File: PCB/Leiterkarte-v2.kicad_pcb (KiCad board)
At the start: 4 copper layers, 69.2 x 70 mm, 56 parts

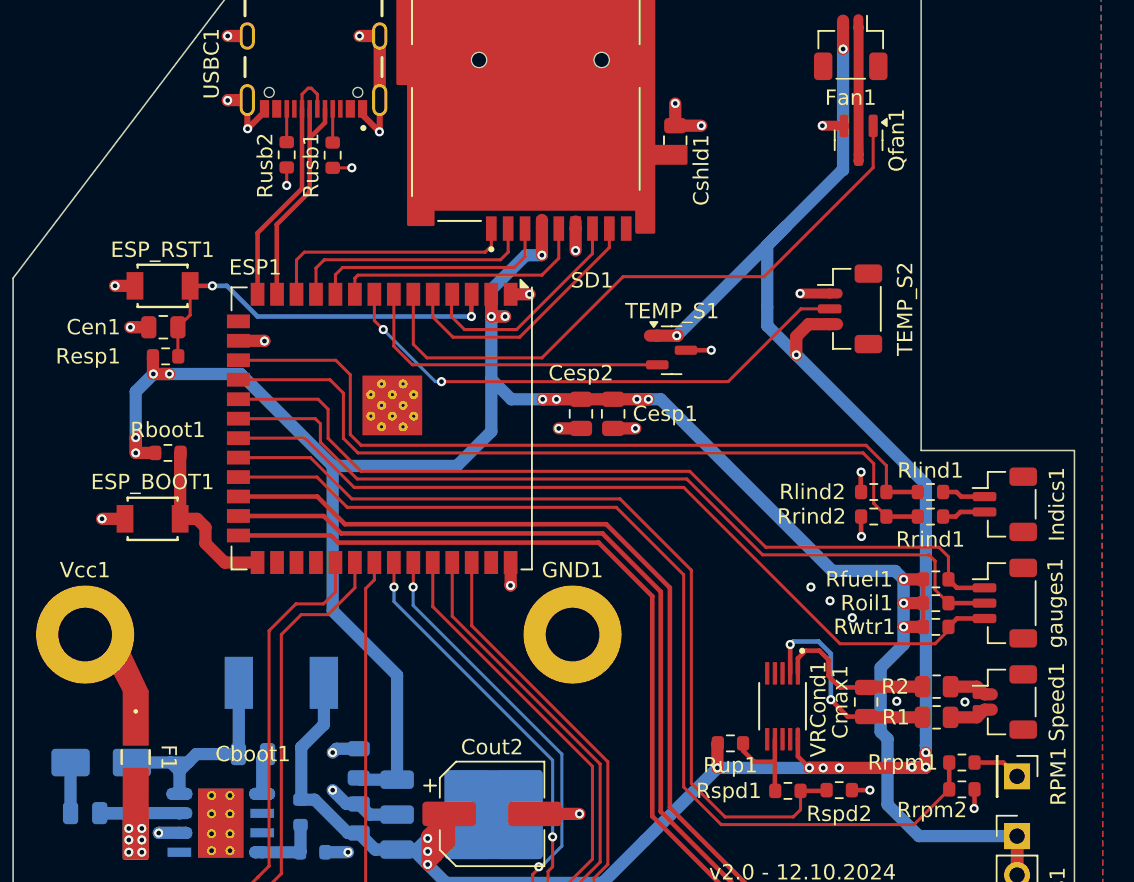
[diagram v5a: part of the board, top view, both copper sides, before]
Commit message: Replaced Fuse;Updated BOM file
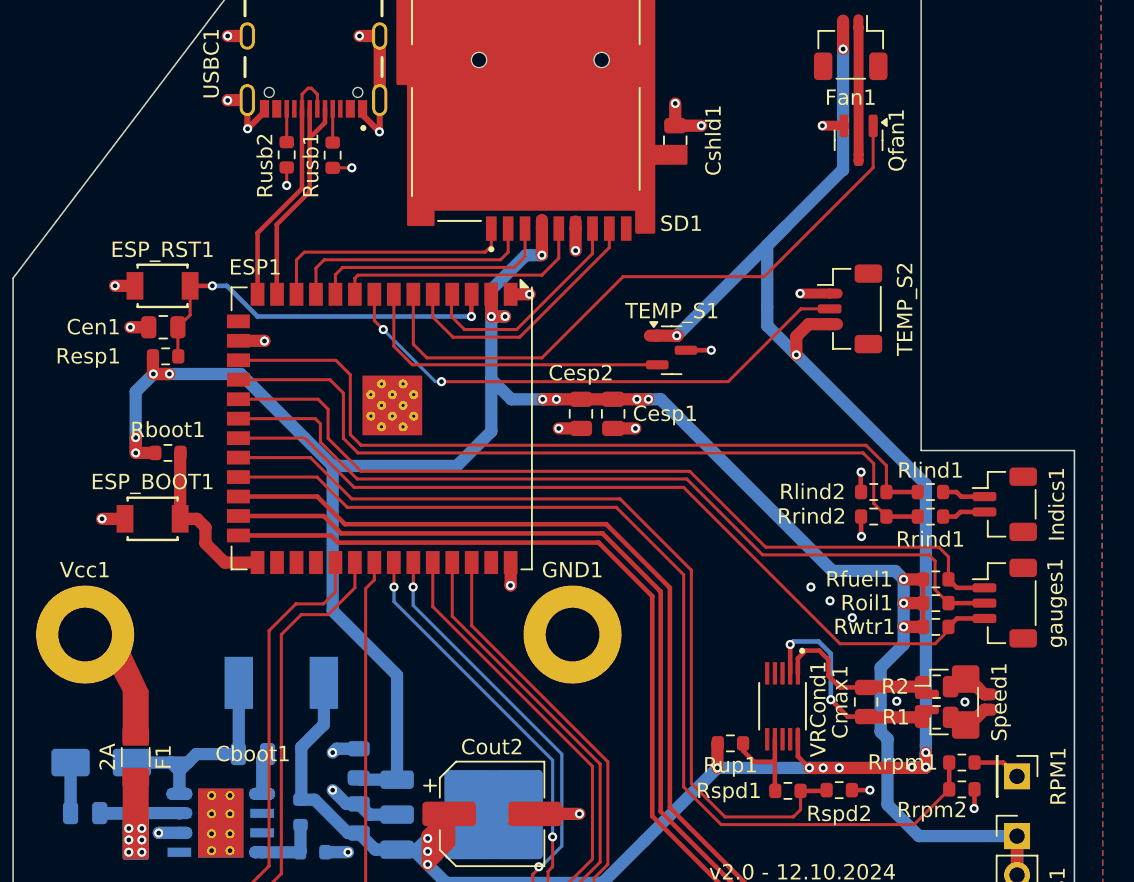
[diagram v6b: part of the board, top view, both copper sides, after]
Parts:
- F1: value 1.5A -> 2A; footprint Fuse:0458Series_LTF-M -> Fuse:Fuse_1206_3216Metric
- moved Speed1 3.75 mm to (146.5, 94.7)
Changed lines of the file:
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@@
 		)
 	)
-	(footprint "Fuse:0458Series_LTF-M"
+	(footprint "Fuse:Fuse_1206_3216Metric"
 		(layer "F.Cu")
 		(at 93.6 98.2468 -90)
-		(tags "0458002.DR ")
+		(descr "Fuse SMD 1206 (3216 Metric), square (rectangular) end terminal, IPC_7351 nominal, (Body size source: http://www.tortai-tech.com/upload/download/2011102023233369053.pdf), generated with kicad-footprint-generator")
+		(tags "fuse")
 		(property "Reference" "F1"
-			(at -0.0032 -2.15 -90)
-			(unlocked yes)
+			(at 0 -1.82 90)
 			(layer "F.SilkS")
 			(effects
@@
 			)
 		)
-		(property "Value" "1.5A"
-			(at 0 0 -90)
-			(unlocked yes)
-			(layer "F.Fab")
+		(property "Value" "2A"
+			(at 0 1.82 90)
+			(layer "F.SilkS")
 			(effects
 				(font
@@
 			)
 		)
-		(property "Footprint" "Fuse:0458Series_LTF-M"
-			(at 0 0 90)
+		(property "Footprint" "Fuse:Fuse_1206_3216Metric"
+			(at 0 0 -90)
+			(unlocked yes)
 			(layer "F.Fab")
 			(hide yes)
@@
 		)
 		(property "Datasheet" ""
-			(at 0 0 90)
+			(at 0 0 -90)
+			(unlocked yes)
 			(layer "F.Fab")
 			(hide yes)
@@
 		)
 		(property "Description" "Fuse"
-			(at 0 0 90)
+			(at 0 0 -90)
+			(unlocked yes)
 			(layer "F.Fab")
 			(hide yes)
@@
 		(attr smd)
 		(fp_line
-			(start -0.457851 0.9144)
-			(end 0.457851 0.9144)
+			(start -0.602064 0.91)
+			(end 0.602064 0.91)
 			(stroke
-				(width 0.1524)
+				(width 0.12)
 				(type solid)
 			)
@@
 		)
 		(fp_line
-			(start 0.457851 -0.9144)
-			(end -0.457851 -0.9144)
-			(stroke
-				(width 0.1524)
-				(type solid)
-			)
-			(layer "F.SilkS")
-		)
-		(fp_circle
-			(center -2.9845 0)
-			(end -2.9083 0)
+			(start -0.602064 -0.91)
+			(end 0.602064 -0.91)
 			(stroke
-				(width 0.1524)
+				(width 0.12)
 				(type solid)
 			)
-			(fill none)
 			(layer "F.SilkS")
 		)
 		(fp_line
-			(start -2.6543 1.3208)
-			(end -2.6543 -1.3208)
+			(start -2.28 1.12)
+			(end -2.28 -1.12)
 			(stroke
-				(width 0.1524)
+				(width 0.05)
 				(type solid)
 			)
@@
 		)
 		(fp_line
-			(start 2.6543 1.3208)
-			(end -2.6543 1.3208)
+			(start 2.28 1.12)
+			(end -2.28 1.12)
 			(stroke
-				(width 0.1524)
+				(width 0.05)
 				(type solid)
 			)
@@
 		)
 		(fp_line
-			(start -2.6543 -1.3208)
-			(end 2.6543 -1.3208)
+			(start -2.28 -1.12)
+			(end 2.28 -1.12)
 			(stroke
-				(width 0.1524)
+				(width 0.05)
 				(type solid)
 			)
@@
 		)
 		(fp_line
-			(start 2.6543 -1.3208)
-			(end 2.6543 1.3208)
+			(start 2.28 -1.12)
+			(end 2.28 1.12)
 			(stroke
-				(width 0.1524)
+				(width 0.05)
 				(type solid)
 			)
@@
 		)
 		(fp_line
-			(start -1.5875 0.7874)
-			(end -0.7747 0.7874)
-			(stroke
-				(width 0.0254)
-				(type solid)
-			)
-			(layer "F.Fab")
-		)
-		(fp_line
-			(start -1.5875 0.7874)
-			(end 1.5875 0.7874)
-			(stroke
-				(width 0.0254)
-				(type solid)
-			)
-			(layer "F.Fab")
-		)
-		(fp_line
-			(start -0.7747 0.7874)
-			(end -0.7747 -0.7874)
-			(stroke
-				(width 0.0254)
-				(type solid)
-			)
-			(layer "F.Fab")
-		)
-		(fp_line
-			(start 0.7747 0.7874)
-			(end 1.5875 0.7874)
-			(stroke
-				(width 0.0254)
-				(type solid)
-			)
-			(layer "F.Fab")
-		)
-		(fp_line
-			(start 1.5875 0.7874)
-			(end 1.5875 -0.7874)
-			(stroke
-				(width 0.0254)
-				(type solid)
-			)
-			(layer "F.Fab")
-		)
-		(fp_line
-			(start 1.5875 0.7874)
-			(end 1.5875 -0.7874)
-			(stroke
-				(width 0.0254)
-				(type solid)
-			)
-			(layer "F.Fab")
-		)
-		(fp_line
-			(start -1.5875 -0.7874)
-			(end -1.5875 0.7874)
+			(start -1.6 0.8)
+			(end -1.6 -0.8)
 			(stroke
-				(width 0.0254)
-				(type solid)
-			)
-			(layer "F.Fab")
-		)
-		(fp_line
-			(start -1.5875 -0.7874)
-			(end -1.5875 0.7874)
-			(stroke
-				(width 0.0254)
-				(type solid)
-			)
-			(layer "F.Fab")
-		)
-		(fp_line
-			(start -0.7747 -0.7874)
-			(end -1.5875 -0.7874)
-			(stroke
-				(width 0.0254)
+				(width 0.1)
 				(type solid)
 			)
@@
 		)
 		(fp_line
-			(start 0.7747 -0.7874)
-			(end 0.7747 0.7874)
+			(start 1.6 0.8)
+			(end -1.6 0.8)
 			(stroke
-				(width 0.0254)
+				(width 0.1)
 				(type solid)
 			)
@@
 		)
 		(fp_line
-			(start 1.5875 -0.7874)
-			(end -1.5875 -0.7874)
+			(start -1.6 -0.8)
+			(end 1.6 -0.8)
 			(stroke
-				(width 0.0254)
+				(width 0.1)
 				(type solid)
 			)
@@
 		)
 		(fp_line
-			(start 1.5875 -0.7874)
-			(end 0.7747 -0.7874)
+			(start 1.6 -0.8)
+			(end 1.6 0.8)
 			(stroke
-				(width 0.0254)
-				(type solid)
-			)
-			(layer "F.Fab")
-		)
-		(fp_circle
-			(center -1.3335 0)
-			(end -1.2573 0)
-			(stroke
-				(width 0.0254)
+				(width 0.1)
 				(type solid)
 			)
-			(fill none)
 			(layer "F.Fab")
 		)
 		(fp_text user "${REFERENCE}"
-			(at 0 0 -90)
-			(unlocked yes)
+			(at 0 0 90)
 			(layer "F.Fab")
 			(effects
 				(font
-					(size 1 1)
-					(thickness 0.15)
+					(size 0.8 0.8)
+					(thickness 0.12)
 				)
 			)
 		)
-		(pad "1" smd rect
-			(at -1.4605 0 270)
-			(size 1.3716 1.6256)
+		(pad "1" smd roundrect
+			(at -1.4 0 270)
+			(size 1.25 1.75)
 			(layers "F.Cu" "F.Paste" "F.Mask")
+			(roundrect_rratio 0.2)
 			(net 42 "Net-(Vcc1-Pin_1)")
 			(pintype "passive")
 		)
-		(pad "2" smd rect
-			(at 1.4605 0 270)
-			(size 1.3716 1.6256)
+		(pad "2" smd roundrect
+			(at 1.4 0 270)
+			(size 1.25 1.75)
 			(layers "F.Cu" "F.Paste" "F.Mask")
+			(roundrect_rratio 0.2)
 			(net 21 "VCC")
 			(pintype "passive")
 		)
-		(zone
-			(net 0)
-			(net_name "")
-			(layer "F.Cu")
-			(hatch full 0.508)
-			(connect_pads
-				(clearance 0)
-			)
-			(min_thickness 0.254)
-			(filled_areas_thickness no)
-			(keepout
-				(tracks not_allowed)
-				(vias not_allowed)
-				(pads allowed)
-				(copperpour not_allowed)
-				(footprints allowed)
-			)
-			(fill
-				(thermal_gap 0.508)
-				(thermal_bridge_width 0.508)
-			)
-			(polygon
-				(pts
-					(xy 94.3366 97.5229) (xy 94.3366 98.9707) (xy 92.8634 98.9707) (xy 92.8634 97.5229)
-				)
-			)
-		)
-		(model "${KIPRJMOD}/Fuse/0458Series_LTF.step"
+		(model "${KICAD8_3DMODEL_DIR}/Fuse.3dshapes/Fuse_1206_3216Metric.wrl"
 			(offset
 				(xyz 0 0 0)
@@
 		(at 119.05 56.0125 180)
 		(property "Reference" "SD1"
-			(at -4.325 -11.135 0)
+			(at -10.15 -7.4375 0)
 			(layer "F.SilkS")
 			(effects
@@
 		(sheetname "Root")
 		(sheetfile "Leiterkarte-v2.kicad_sch")
-		(attr exclude_from_pos_files)
 		(fp_circle
 			(center 0 0)
@@
 	(footprint "Connector_JST:JST_SH_BM02B-SRSS-TB_1x02-1MP_P1.00mm_Vertical"
 		(layer "F.Cu")
-		(at 150.3 94.65 -90)
+		(at 146.549008 94.65 -90)
 		(descr "JST SH series connector, BM02B-SRSS-TB (http://www.jst-mfg.com/product/pdf/eng/eSH.pdf), generated with kicad-footprint-generator")
 		(tags "connector JST SH vertical")
@@
 		(tags "capacitor")
 		(property "Reference" "Cshld1"
-			(at 1.95 -1.7 -90)
+			(at 0 -2.5 -90)
 			(layer "F.SilkS")
 			(effects
@@
 		(sheetname "Root")
 		(sheetfile "Leiterkarte-v2.kicad_sch")
-		(attr exclude_from_pos_files)
 		(fp_circle
 			(center 0 0)
@@
 		(height -6.357359)
 		(gr_text "40.0000 mm"
-			(at 160.05 98.242641 90)
+			(at 147.335282 98.242641 90)
 			(layer "Dwgs.User")
 			(effects

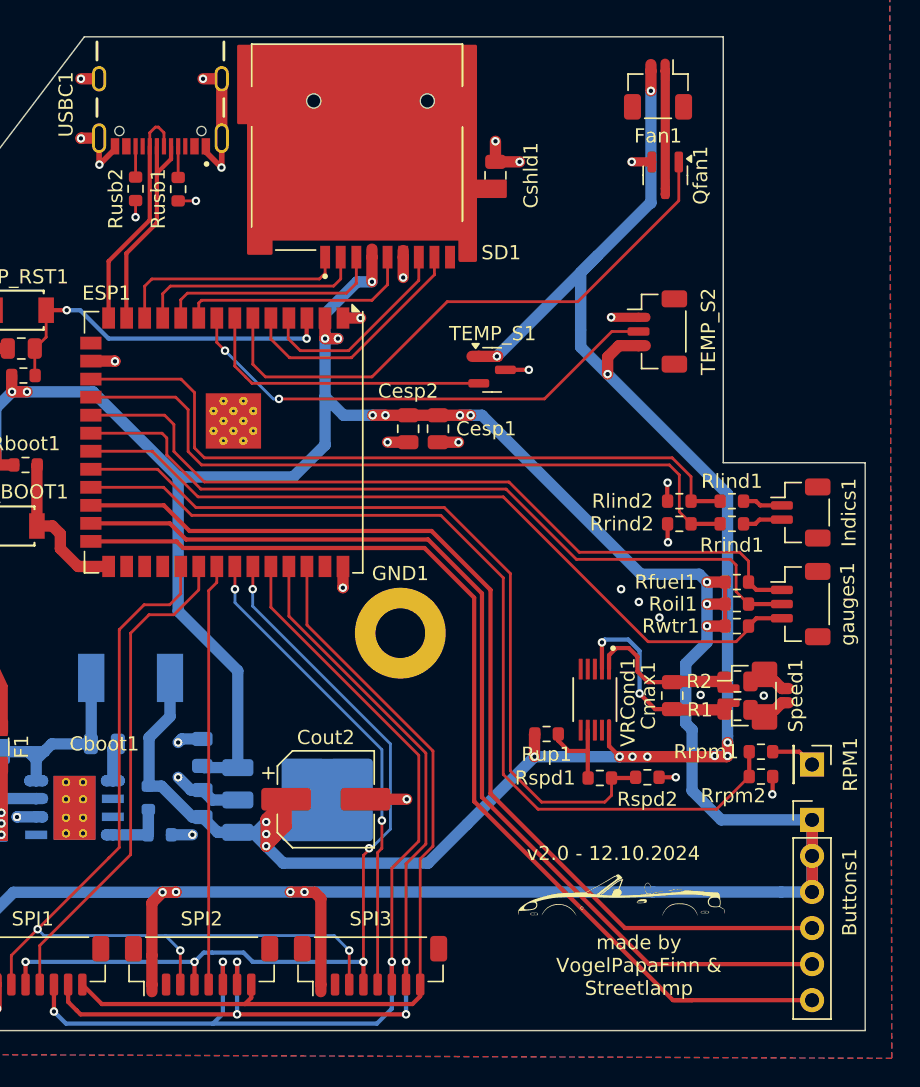
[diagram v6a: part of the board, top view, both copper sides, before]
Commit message: Added pulldown resistors for the buttons;Changed input GPIof button 3;Replaced a few capacitors (BOM); Put temperature sensors on the 3.3V line
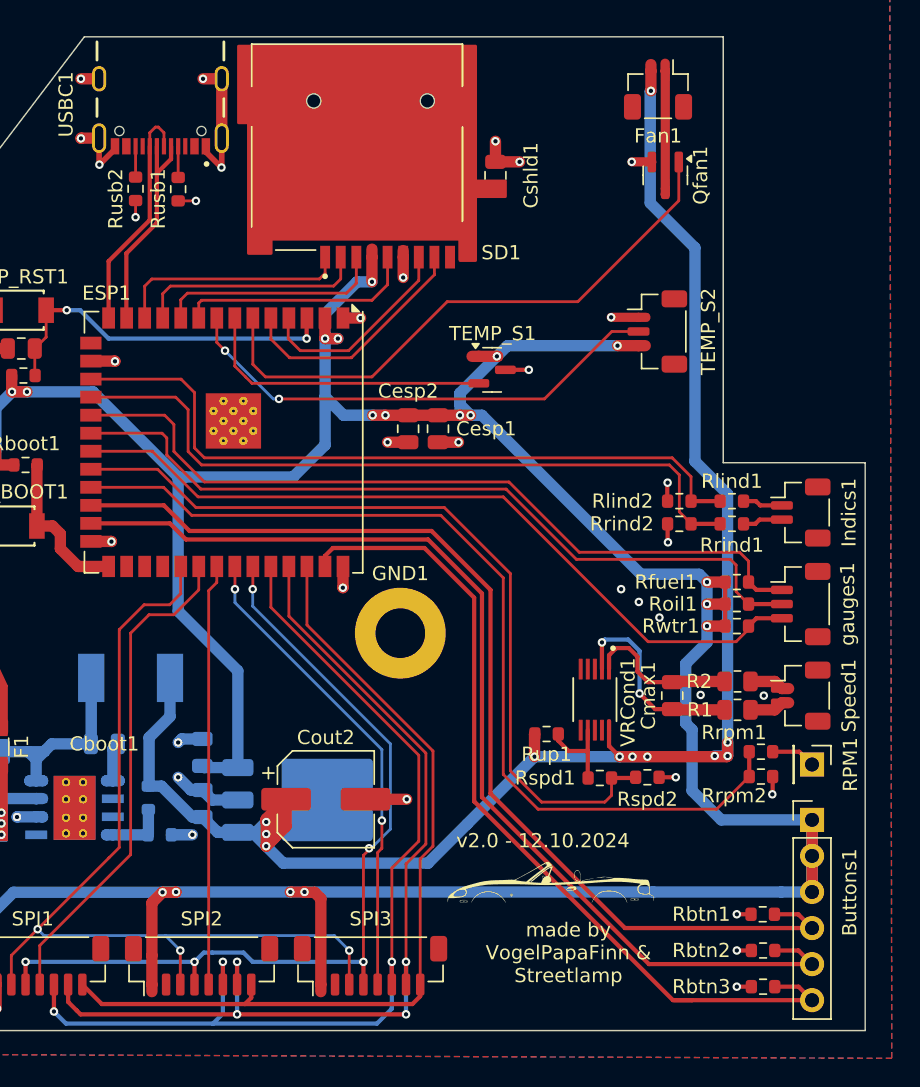
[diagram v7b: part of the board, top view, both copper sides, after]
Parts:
- added Rbtn1: 10k, Resistor_SMD:R_0603_1608Metric, F.Cu at (147.6, 110.0)
- added Rbtn2: 10k, Resistor_SMD:R_0603_1608Metric, F.Cu at (147.7, 112.6)
- added Rbtn3: 10k, Resistor_SMD:R_0603_1608Metric, F.Cu at (147.7, 115.2)
- Cin2: value 10uF -> 1uF
- Cout1: value 22uF -> 2.2uF
- moved G*** 5.04 mm to (132.7, 107.3)
- moved Speed1 3.75 mm to (150.3, 94.7)
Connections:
- ESP1 pad 26: Button3 -> GND
- ESP1 pad 39: unconnected-(ESP1-IO1-Pad39) -> Button3
- TEMP_S1 pad 1: +5V -> +3.3V
- TEMP_S2 pad 3: +5V -> +3.3V
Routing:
- net +5V: track 151.0 -> 130.8 mm, vias 13 -> 11
- net +3.3V: track 243.8 -> 263.5 mm, vias 20 -> 22
- net Button3: track 73.8 -> 61.1 mm
- net GND: track 75.6 -> 80.1 mm, vias 36 -> 40
- net Button1: track 71.5 -> 74.6 mm
- net Button2: track 72.1 -> 75.1 mm
